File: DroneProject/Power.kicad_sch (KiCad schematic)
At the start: 27 parts, among them Q31 RJK0654DPB-00-J5, SW31 PTS815 SJM 250 SMTR LFS, U31 AP63203WU, U32 SN74LVC1G08DBVR

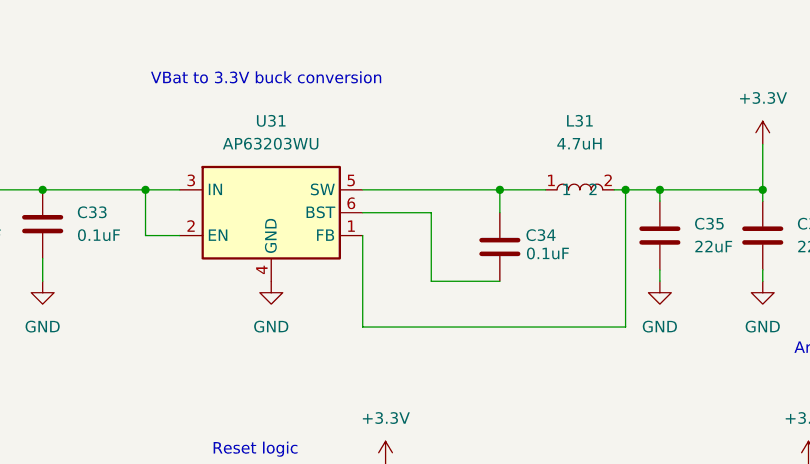
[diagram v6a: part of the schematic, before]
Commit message: Finished layout for controller board
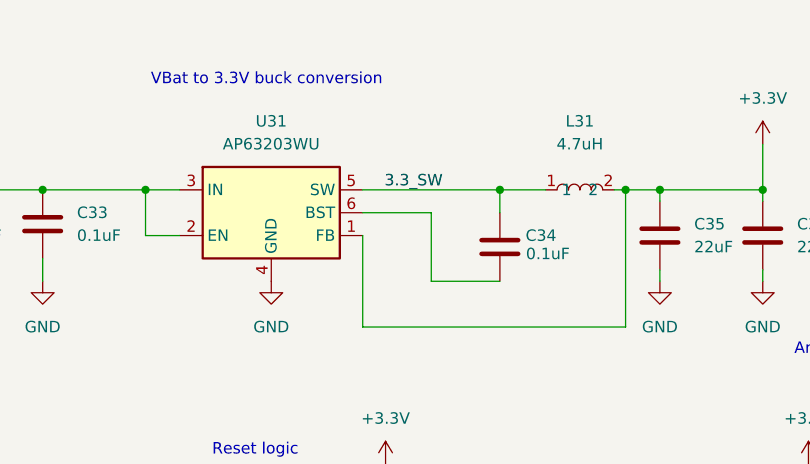
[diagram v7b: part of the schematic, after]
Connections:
- net 3.3_SW: now reaches C34.2, L31.1, U31.5 (SW)
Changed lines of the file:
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@@
+		)
+	)
+	(label "3.3_SW"
+		(at 133.35 43.18 180)
+		(effects
+			(font
+				(size 1.27 1.27)
+			)
+			(justify right bottom)
 		)
 	)
